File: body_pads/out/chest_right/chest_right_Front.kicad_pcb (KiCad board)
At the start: 2 copper layers, 165.5 x 206.5 mm, 0 parts

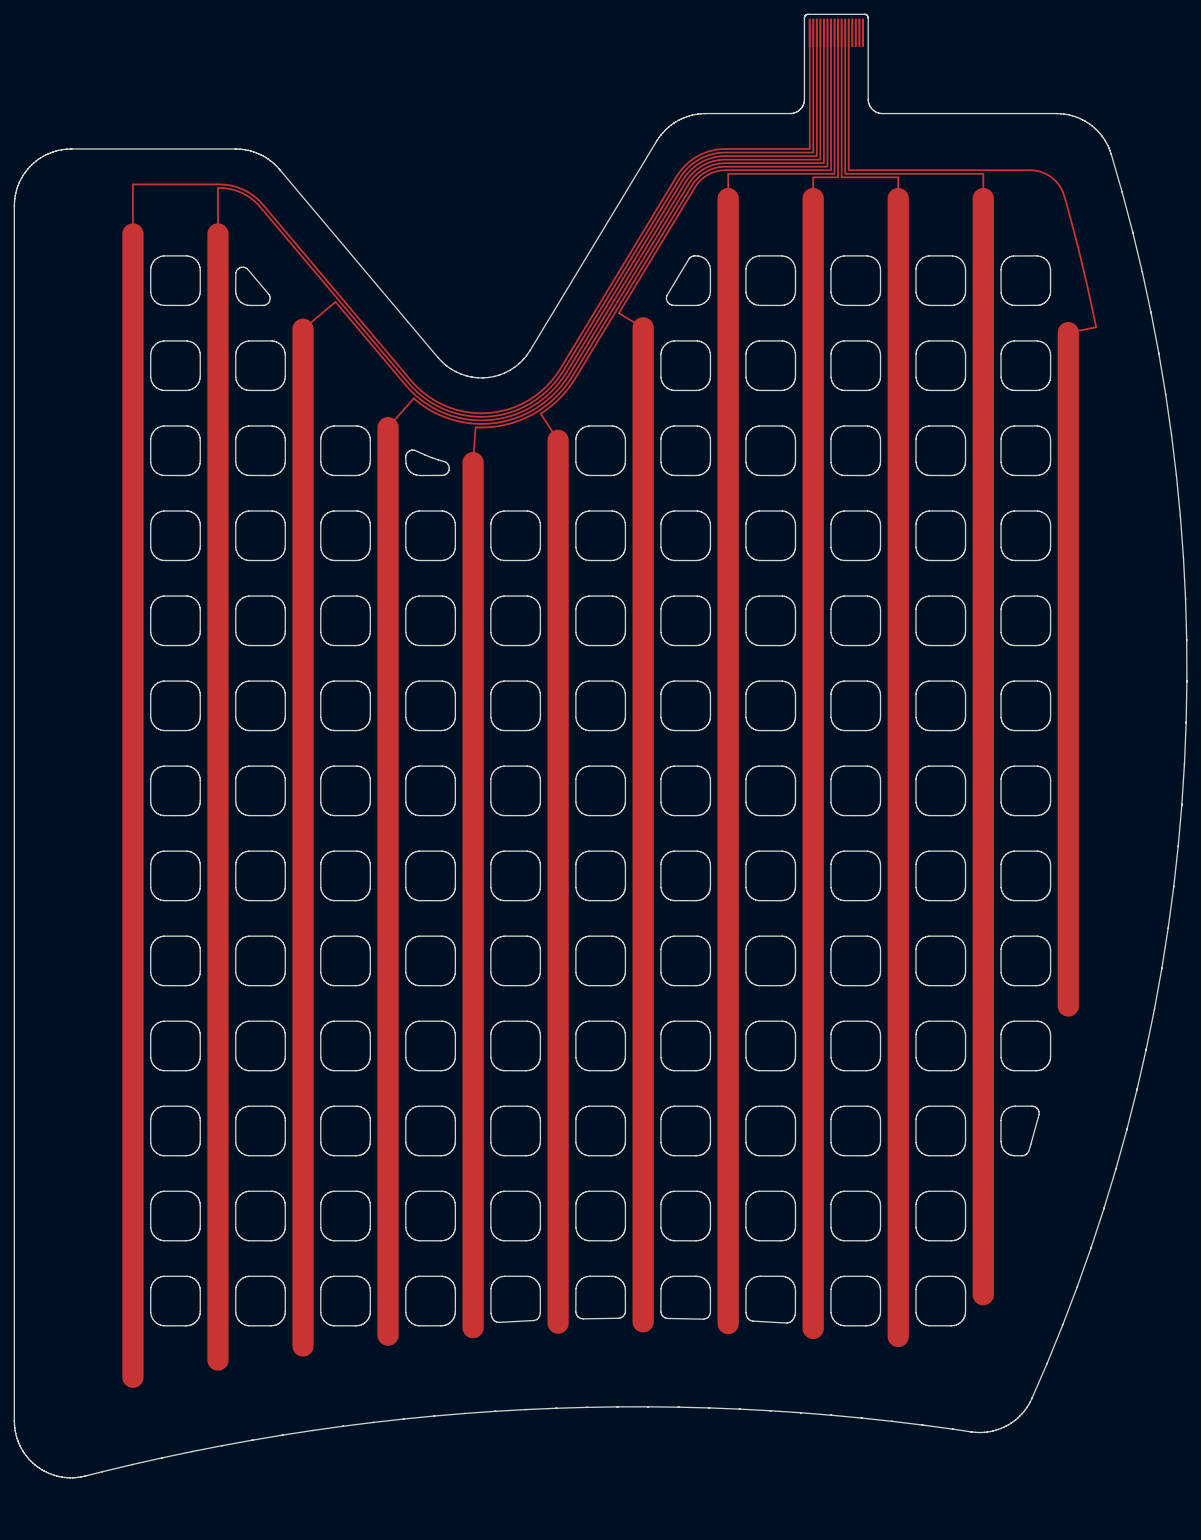
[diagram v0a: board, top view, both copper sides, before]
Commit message: Terminate body pads with vias and an FFC connector; export the full Gerber set
The pad tails now follow README Step 5 like the glove: every electrode trace
ends in a through via (0.45/0.2 mm, two staggered rows) and a 16-pin 0.5 mm
FFC connector (KiCad library Hirose FH12-16S-0.5SH) sits on the side opposite
the electrodes, making each board a 2-layer flex. A nested staircase fans the
0.5 mm bus out to the 1.0 mm via pitch and back to the 0.5 mm pads without
crossings. body_pads/kicad_post.py runs with KiCad's own python to add the
vias, footprint, connector-side tracks and nets; a .kicad_pro with flex rules
is written so kicad-cli DRC checks the right limits, and the Gerber export now
produces the same file set as the glove (both copper layers, mask, paste,
silkscreen, edge cuts, Eco1/Eco2, PTH/NPTH drills and maps).

Also: the column grid is shifted so no column exits under the tail bus, the
mirrored chest half swaps its tail order so both halves match, previews gain
a tail close-up, and the README describes the new tail, layers and checks.
Includes the body-pad documentation docx added to the working tree.

Co-Authored-By: Claude Fable 5.1 <noreply@anthropic.com>
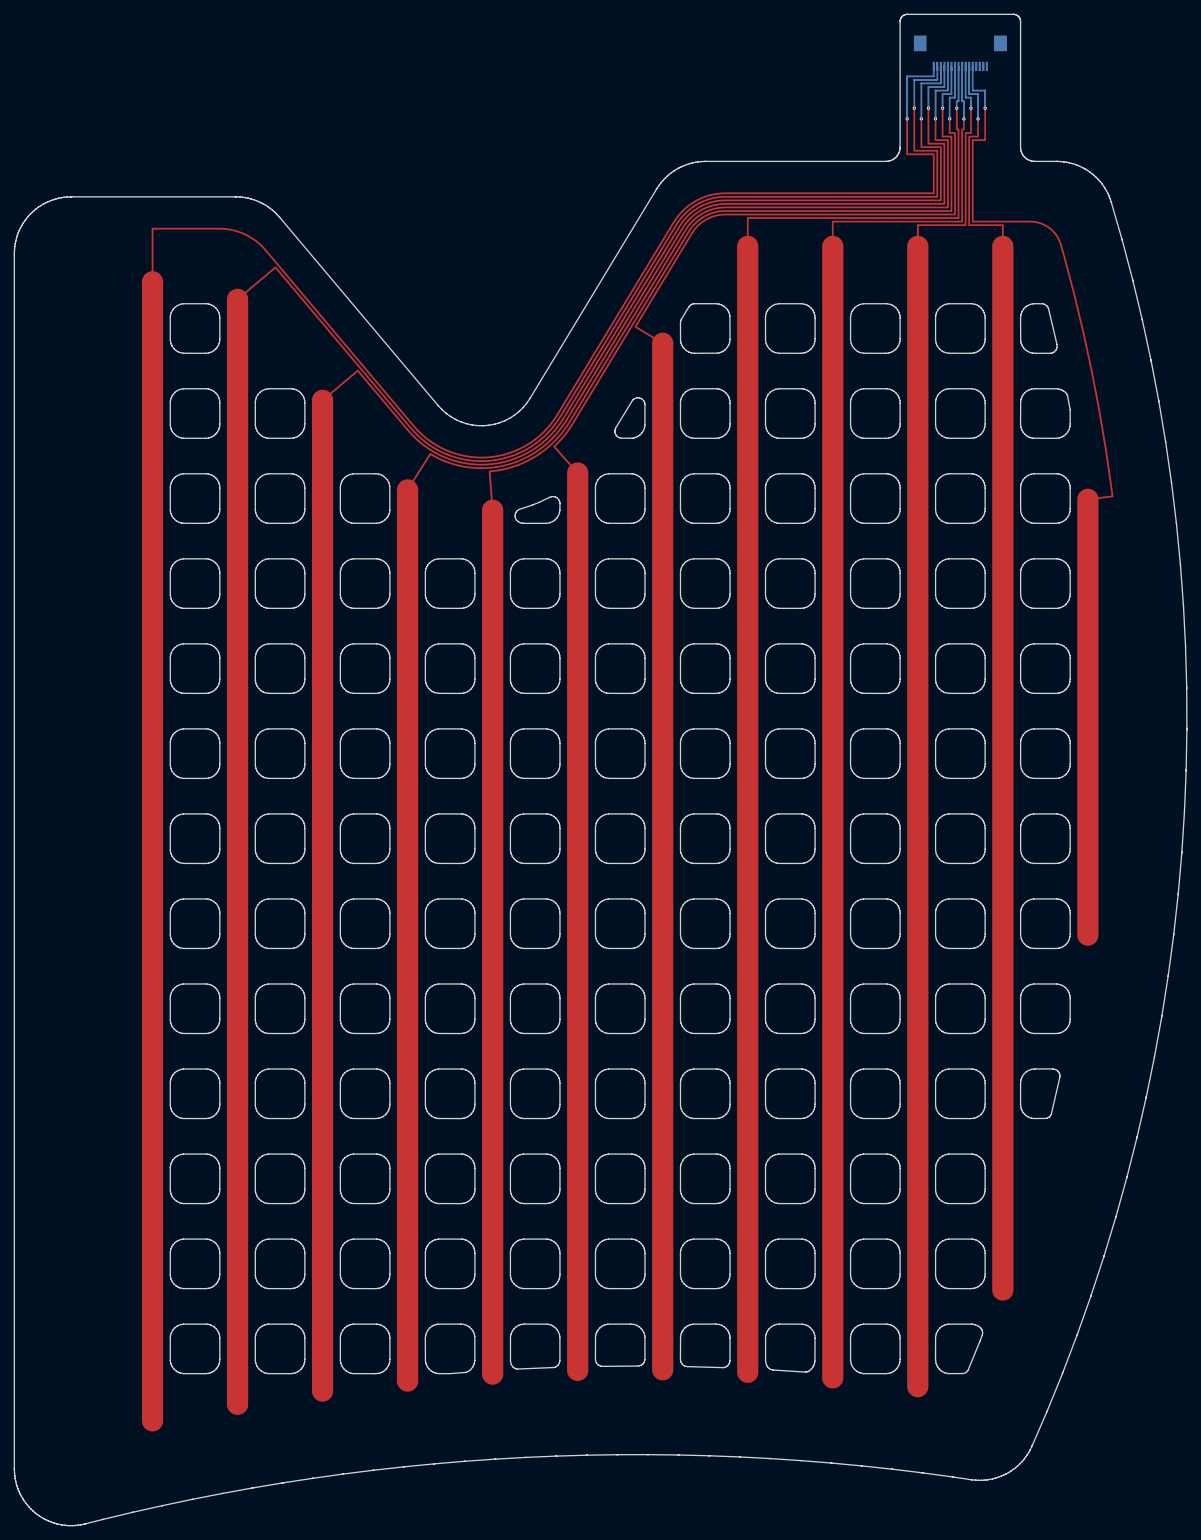
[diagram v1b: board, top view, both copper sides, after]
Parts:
- added J1: Hirose_FH12-16S-0.5SH_1x16-1MP_P0.50mm_Horizontal, Hirose_FH12-16S-0.5SH_1x16-1MP_P0.50mm_Horizontal, B.Cu at (143.5, 15.5)
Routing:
- net COL00: track 0.00 -> 11.2 mm, vias 0 -> 1
- net COL02: track 0.00 -> 10.2 mm, vias 0 -> 1
- net COL04: track 0.00 -> 9.15 mm, vias 0 -> 1
- net COL01: track 0.00 -> 9.15 mm, vias 0 -> 1
- net COL10: track 0.00 -> 8.65 mm, vias 0 -> 1
- net COL06: track 0.00 -> 8.15 mm, vias 0 -> 1
- net COL03: track 0.00 -> 8.15 mm, vias 0 -> 1
- net COL11: track 0.00 -> 7.65 mm, vias 0 -> 1
- net COL08: track 0.00 -> 7.65 mm, vias 0 -> 1
- net COL05: track 0.00 -> 7.15 mm, vias 0 -> 1
- net COL09: track 0.00 -> 6.65 mm, vias 0 -> 1
- net COL07: track 0.00 -> 6.15 mm, vias 0 -> 1
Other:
- board size 165.5 x 206.5 mm -> 165.5 x 213.3 mm
- board text added: "chest_right Front"
- board text added: "chest_right Front: 2-layer flex. Electrodes on F.Cu under the F.Mask opening; FFC connector J1 on B.Cu. Eco1.User = PSA adhesive on the F.Cu side. Eco2.User = stiffener under the connector (on the F.Cu side of the tail)."
- board text removed: "chest_right Front: 1-layer flex, copper on F.Cu. F.Mask = coverlay openings. Eco1.User = PSA adhesive (copper side). Eco2.User = tail stiffener (opposite side), total tail 0.30 +/-0.05 mm. 16-pin 0.5 mm FFC fingers."
